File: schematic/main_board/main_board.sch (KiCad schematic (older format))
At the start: 13 parts, among them J1 Line OUT, J2 Line IN, P1 +Vref, P2 GND, P3 -Vref, P4 Probe, P5 GND, U1 LM324N

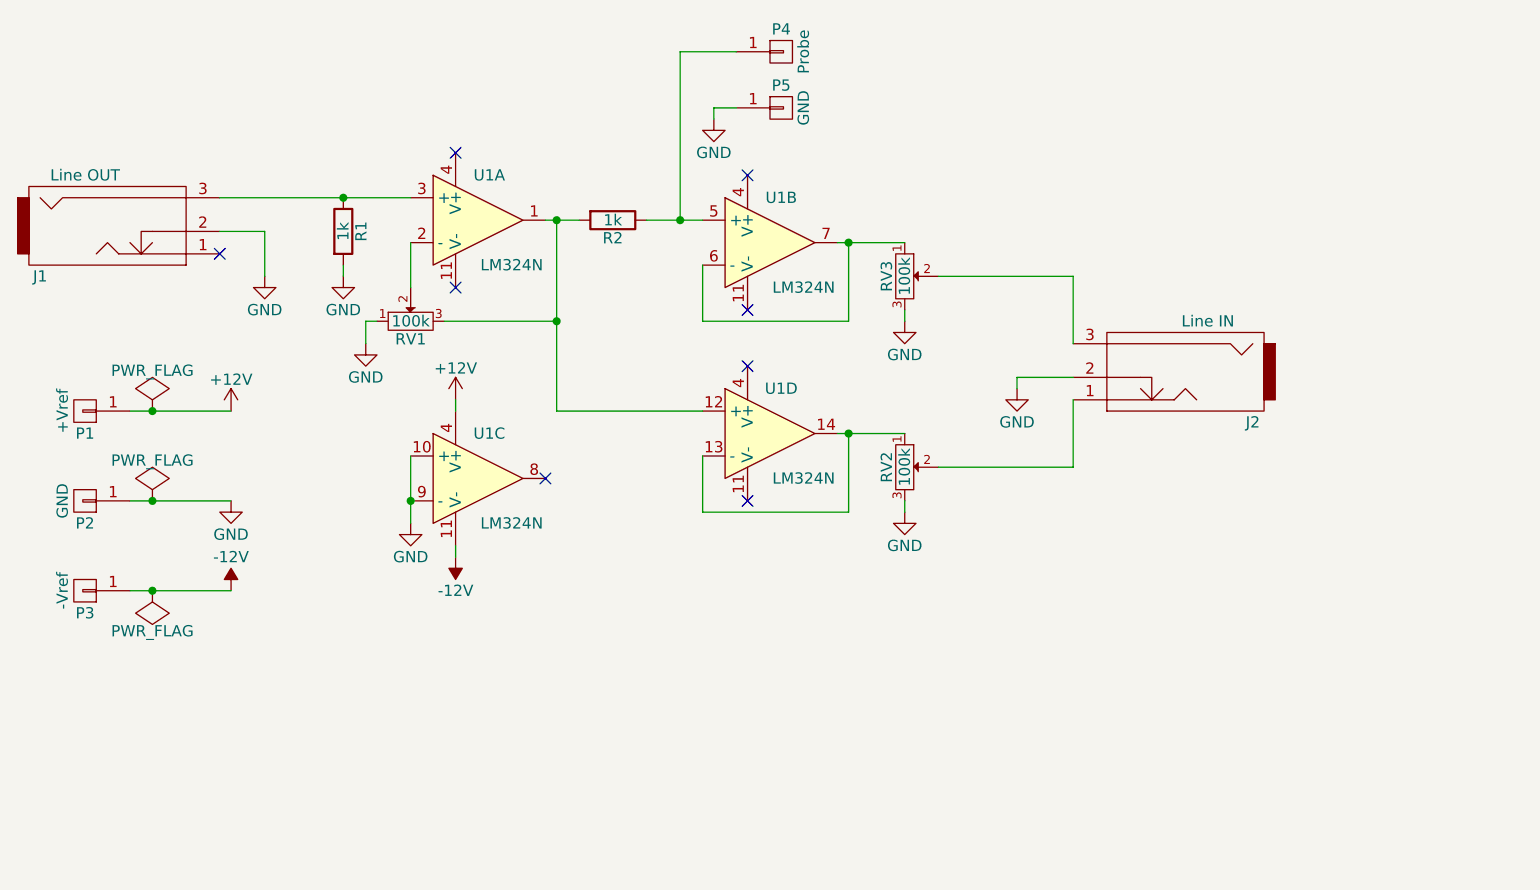
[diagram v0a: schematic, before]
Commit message: Add footprint for potentiometer.
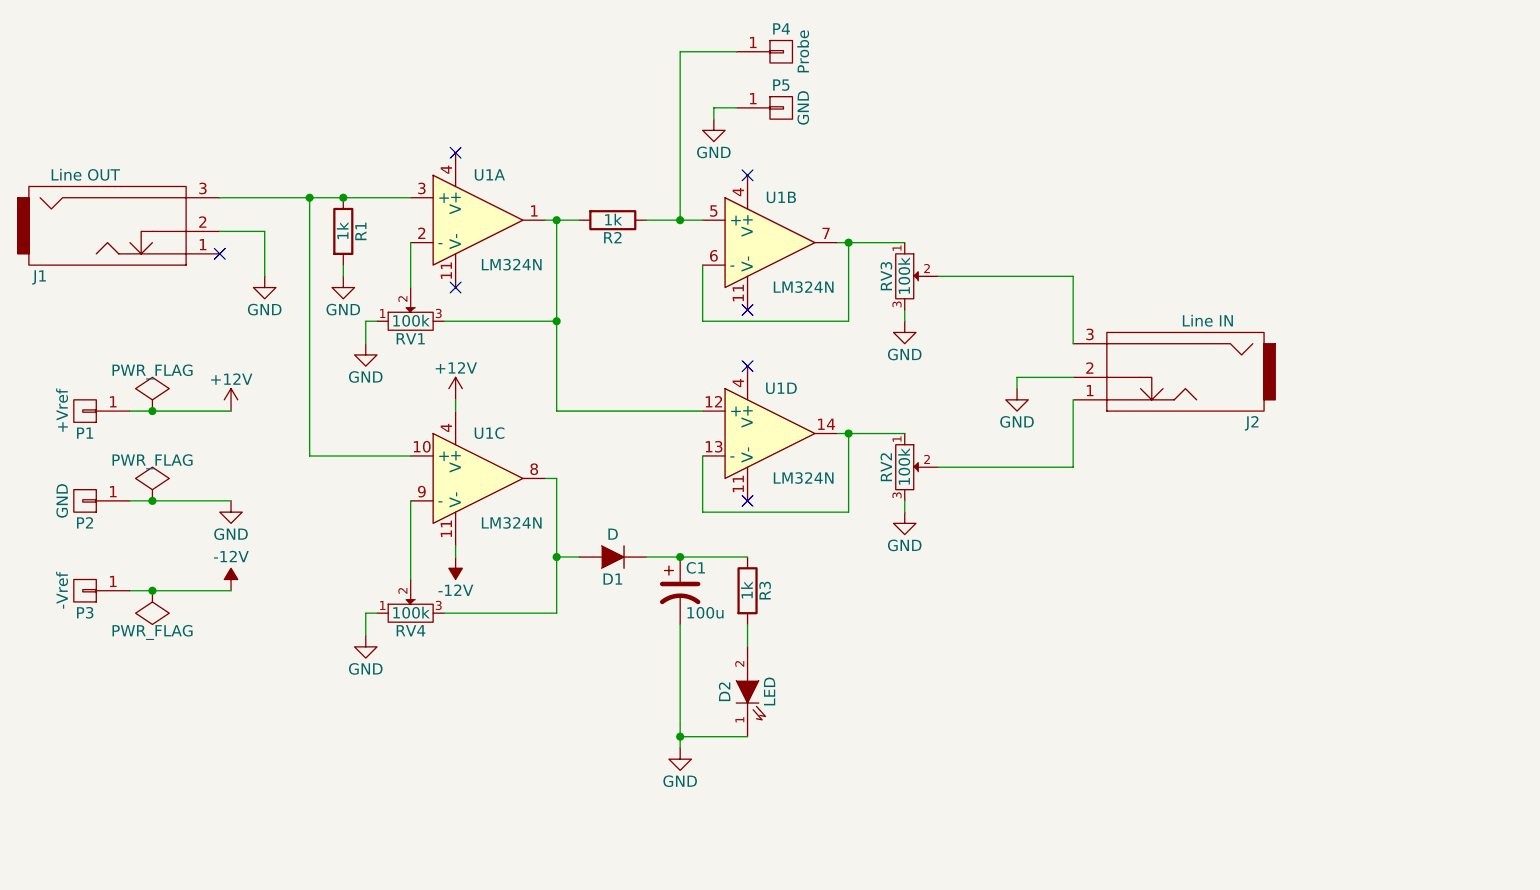
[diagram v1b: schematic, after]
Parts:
- added C1: 100u, symbol CP1
- added D1: D, symbol D
- added D2: LED, symbol LED
- added R3: 1k, footprints:Resistor_Horizontal_RM20mm_0.25W, symbol R
- added RV4: 100k, footprints:Potentiometer_CP3-36, symbol POT
- RV1, RV2, RV3: footprint Potentiometers:Potentiometer_Bourns_3005_Angular_ScrewFront -> footprints:Potentiometer_CP3-36
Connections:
- net GND: now also C1.2, D2.1 (K), RV4.1; no longer U1.10 (+), U1.9 (-)
- net at J1.3, R1.1, U1.3 (+): now also U1.10 (+)
- net at U1.8: now also D1.2 (A), RV4.3
- new net: RV4.2, U1.9 (-)
- new net: C1.1, D1.1 (K), R3.1
- new net: D2.2 (A), R3.2
- no-connect marks 8 -> 7
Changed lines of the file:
@@
 	1    0    0    -1
 $EndComp
-NoConn ~ 4000 3700
 $Comp
 L GND #PWR01
 U 1 1 57BD55DE
-P 3400 3900
-F 0 "#PWR01" H 3400 3650 50  0001 C CNN
-F 1 "GND" H 3400 3750 50  0000 C CNN
-F 2 "" H 3400 3900 50  0000 C CNN
-F 3 "" H 3400 3900 50  0000 C CNN
-	1    3400 3900
+P 3200 4400
+F 0 "#PWR01" H 3200 4150 50  0001 C CNN
+F 1 "GND" H 3200 4250 50  0000 C CNN
+F 2 "" H 3200 4400 50  0000 C CNN
+F 3 "" H 3200 4400 50  0000 C CNN
+	1    3200 4400
 	1    0    0    -1
 $EndComp
@@
 F 0 "RV1" H 3400 2920 50  0000 C CNN
 F 1 "100k" H 3400 3000 50  0000 C CNN
-F 2 "Potentiometers:Potentiometer_Bourns_3005_Angular_ScrewFront" H 3400 3000 50  0001 C CNN
+F 2 "footprints:Potentiometer_CP3-36" H 3400 3000 50  0001 C CNN
 F 3 "" H 3400 3000 50  0000 C CNN
 	1    3400 3000
@@
 F 0 "RV3" H 5600 2720 50  0000 C CNN
 F 1 "100k" H 5600 2800 50  0000 C CNN
-F 2 "Potentiometers:Potentiometer_Bourns_3005_Angular_ScrewFront" H 5600 2800 50  0001 C CNN
+F 2 "footprints:Potentiometer_CP3-36" H 5600 2800 50  0001 C CNN
 F 3 "" H 5600 2800 50  0000 C CNN
 	1    5600 2800
@@
 F 0 "RV2" H 5600 3570 50  0000 C CNN
 F 1 "100k" H 5600 3650 50  0000 C CNN
-F 2 "Potentiometers:Potentiometer_Bourns_3005_Angular_ScrewFront" H 5600 3650 50  0001 C CNN
+F 2 "footprints:Potentiometer_CP3-36" H 5600 3650 50  0001 C CNN
 F 3 "" H 5600 3650 50  0000 C CNN
 	1    5600 3650
@@
 	1    0    0    -1
 $EndComp
-Wire Wire Line
-	5300 2650 5600 2650
-Wire Wire Line
-	4700 2750 4700 3000
-Wire Wire Line
-	4700 3000 5350 3000
-Wire Wire Line
-	5350 3000 5350 2650
-Connection ~ 5350 2650
-Wire Wire Line
-	5600 3500 5300 3500
-Wire Wire Line
-	4700 3600 4700 3850
-Wire Wire Line
-	4700 3850 5350 3850
-Wire Wire Line
-	5350 3850 5350 3500
-Connection ~ 5350 3500
-Wire Wire Line
-	5600 3800 5600 3850
-Wire Wire Line
-	3400 2650 3400 2850
-Wire Wire Line
-	3550 3000 4050 3000
 $Comp
 L GND #PWR04
@@
 	1    0    0    -1
 $EndComp
-Wire Wire Line
-	3200 3100 3200 3000
-Wire Wire Line
-	3200 3000 3250 3000
 $Comp
 L GND #PWR05
@@
 	1    0    0    -1
 $EndComp
-Wire Wire Line
-	3100 2750 3100 2800
-Wire Wire Line
-	2550 2450 3400 2450
-Wire Wire Line
-	4700 2550 4450 2550
-Wire Wire Line
-	4000 2550 4150 2550
-Wire Wire Line
-	4050 2550 4050 3400
-Connection ~ 4050 2550
-Wire Wire Line
-	4050 3400 4700 3400
-Connection ~ 4050 3000
 NoConn ~ 3600 2850
 NoConn ~ 3600 2250
@@
 	-1   0    0    1
 $EndComp
-Wire Wire Line
-	5600 3000 5600 2950
-Wire Wire Line
-	3600 4000 3600 4050
-Wire Wire Line
-	3600 3400 3600 3350
-Wire Wire Line
-	3400 3600 3400 3900
-Connection ~ 3400 3800
 $Comp
 L PWR_FLAG #FLG07
@@
 	1    0    0    -1
 $EndComp
-Wire Wire Line
-	2150 3400 2600 3400
-Connection ~ 2250 3400
 $Comp
 L GND #PWR09
@@
 $EndComp
 $Comp
-L -12V #PWR4
+L -12V #PWR3
 U 1 1 57BD83A0
 P 2600 4200
-F 0 "#PWR4" H 2600 4300 50  0001 C CNN
+F 0 "#PWR3" H 2600 4300 50  0001 C CNN
 F 1 "-12V" H 2600 4350 50  0000 C CNN
 F 2 "" H 2600 4200 50  0000 C CNN
@@
 	-1   0    0    1
 $EndComp
-Wire Wire Line
-	2150 4200 2600 4200
-Connection ~ 2250 4200
-Wire Wire Line
-	2150 3800 2600 3800
-Connection ~ 2250 3800
 $Comp
 L CONN_01X01 P4
@@
 	1    0    0    -1
 $EndComp
-Wire Wire Line
-	4850 2050 4750 2050
-Wire Wire Line
-	4750 2050 4750 2100
-Wire Wire Line
-	4600 1800 4600 2550
-Connection ~ 4600 2550
-Wire Wire Line
-	4850 1800 4600 1800
 $Comp
 L JACK_2P J1
@@
 	1    0    0    -1
 $EndComp
+$Comp
+L D D1
+U 1 1 57C3D329
+P 4300 4050
+F 0 "D1" H 4300 4150 50  0000 C CNN
+F 1 "D" H 4300 3950 50  0000 C CNN
+F 2 "" H 4300 4050 50  0001 C CNN
+F 3 "" H 4300 4050 50  0000 C CNN
+	1    4300 4050
+	-1   0    0    1
+$EndComp
+$Comp
+L R R3
+U 1 1 57C3D3FD
+P 4900 4200
+F 0 "R3" V 4980 4200 50  0000 C CNN
+F 1 "1k" V 4900 4200 50  0000 C CNN
+F 2 "footprints:Resistor_Horizontal_RM20mm_0.25W" V 4830 4200 50  0001 C CNN
+F 3 "" H 4900 4200 50  0000 C CNN
+	1    4900 4200
+	1    0    0    -1
+$EndComp
+$Comp
+L CP1 C1
+U 1 1 57C3D44E
+P 4600 4200
+F 0 "C1" H 4625 4300 50  0000 L CNN
+F 1 "100u" H 4625 4100 50  0000 L CNN
+F 2 "" H 4600 4200 50  0001 C CNN
+F 3 "" H 4600 4200 50  0000 C CNN
+	1    4600 4200
+	1    0    0    -1
+$EndComp
+$Comp
+L LED D2
+U 1 1 57C3D493
+P 4900 4650
+F 0 "D2" H 4900 4750 50  0000 C CNN
+F 1 "LED" H 4900 4550 50  0000 C CNN
+F 2 "" H 4900 4650 50  0001 C CNN
+F 3 "" H 4900 4650 50  0000 C CNN
+	1    4900 4650
+	0    -1   -1   0
+$EndComp
+$Comp
+L POT RV4
+U 1 1 57C3E022
+P 3400 4300
+F 0 "RV4" H 3400 4220 50  0000 C CNN
+F 1 "100k" H 3400 4300 50  0000 C CNN
+F 2 "footprints:Potentiometer_CP3-36" H 3400 4300 50  0001 C CNN
+F 3 "" H 3400 4300 50  0000 C CNN
+	1    3400 4300
+	1    0    0    -1
+$EndComp
+$Comp
+L GND #PWR015
+U 1 1 57C3EFA0
+P 4600 4900
+F 0 "#PWR015" H 4600 4650 50  0001 C CNN
+F 1 "GND" H 4600 4750 50  0000 C CNN
+F 2 "" H 4600 4900 50  0000 C CNN
+F 3 "" H 4600 4900 50  0000 C CNN
+	1    4600 4900
+	1    0    0    -1
+$EndComp
+Wire Wire Line
+	5300 2650 5600 2650
+Wire Wire Line
+	4700 2750 4700 3000
+Wire Wire Line
+	4700 3000 5350 3000
+Wire Wire Line
+	5350 3000 5350 2650
+Connection ~ 5350 2650
+Wire Wire Line
+	5600 3500 5300 3500
+Wire Wire Line
+	4700 3600 4700 3850
+Wire Wire Line
+	4700 3850 5350 3850
+Wire Wire Line
+	5350 3850 5350 3500
+Connection ~ 5350 3500
+Wire Wire Line
+	5600 3800 5600 3850
+Wire Wire Line
+	3400 2650 3400 2850
+Wire Wire Line
+	3550 3000 4050 3000
+Wire Wire Line
+	3200 3100 3200 3000
+Wire Wire Line
+	3200 3000 3250 3000
+Wire Wire Line
+	3100 2750 3100 2800
+Wire Wire Line
+	2550 2450 3400 2450
+Wire Wire Line
+	4700 2550 4450 2550
+Wire Wire Line
+	4000 2550 4150 2550
+Wire Wire Line
+	4050 2550 4050 3400
+Connection ~ 4050 2550
+Wire Wire Line
+	4050 3400 4700 3400
+Connection ~ 4050 3000
+Wire Wire Line
+	5600 3000 5600 2950
+Wire Wire Line
+	3600 4000 3600 4050
+Wire Wire Line
+	3600 3400 3600 3350
+Wire Wire Line
+	2150 3400 2600 3400
+Connection ~ 2250 3400
+Wire Wire Line
+	2150 4200 2600 4200
+Connection ~ 2250 4200
+Wire Wire Line
+	2150 3800 2600 3800
+Connection ~ 2250 3800
+Wire Wire Line
+	4850 2050 4750 2050
+Wire Wire Line
+	4750 2050 4750 2100
+Wire Wire Line
+	4600 1800 4600 2550
+Connection ~ 4600 2550
+Wire Wire Line
+	4850 1800 4600 1800
 Wire Wire Line
 	6350 3250 6100 3250
@@
 	2750 2600 2550 2600
 Connection ~ 3100 2450
+Wire Wire Line
+	3400 3800 3400 4150
+Wire Wire Line
+	3200 4400 3200 4300
+Wire Wire Line
+	3200 4300 3250 4300
+Wire Wire Line
+	3550 4300 4050 4300
+Wire Wire Line
+	4050 4300 4050 3700
+Wire Wire Line
+	4050 3700 4000 3700
+Wire Wire Line
+	2950 2450 2950 3600
+Wire Wire Line
+	2950 3600 3400 3600
+Connection ~ 2950 2450
+Wire Wire Line
+	4150 4050 4050 4050
+Connection ~ 4050 4050
+Wire Wire Line
+	4450 4050 4900 4050
+Connection ~ 4600 4050
+Wire Wire Line
+	4900 4350 4900 4450
+Wire Wire Line
+	4900 4850 4600 4850
+Wire Wire Line
+	4600 4350 4600 4900
+Connection ~ 4600 4850
 $EndSCHEMATC

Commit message: Added circuit to schematic for limit output voltage range.
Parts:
- added D3, D4, D5, D6: D, symbol D
- added R4, R5: 1k, symbol R
- J1: value Line OUT -> To Line OUT
- J2: value Line IN -> To Line IN
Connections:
- net GND: now also RV2.1, RV3.1, D3.1 (K), D4.1 (K), D5.2 (A), D6.2 (A); no longer RV2.3, RV3.3
- net at U1.6 (-), U1.7: now also RV3.3; no longer RV3.1
- net at U1.13 (-), U1.14: now also RV2.3; no longer RV2.1
- net at RV3.2: now also R4.2; no longer J2.3
- net at RV2.2: now also R5.2; no longer J2.1
- new net: D4.2 (A), D6.1 (K), J2.1, R5.1
- new net: D3.2 (A), D5.1 (K), J2.3, R4.1
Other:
- moved on the sheet: J2
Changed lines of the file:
@@
 $EndComp
 $Comp
-L GND #PWR01
+L GND #PWR7
 U 1 1 57BD55DE
 P 3200 4400
-F 0 "#PWR01" H 3200 4150 50  0001 C CNN
+F 0 "#PWR7" H 3200 4150 50  0001 C CNN
 F 1 "GND" H 3200 4250 50  0000 C CNN
 F 2 "" H 3200 4400 50  0000 C CNN
@@
 F 3 "" H 5600 2800 50  0000 C CNN
 	1    5600 2800
-	0    1    1    0
+	0    1    -1   0
 $EndComp
 $Comp
@@
 F 3 "" H 5600 3650 50  0000 C CNN
 	1    5600 3650
-	0    1    1    0
-$EndComp
-$Comp
-L GND #PWR02
+	0    1    -1   0
+$EndComp
+$Comp
+L GND #PWR12
 U 1 1 57BD5FBC
 P 5600 3000
-F 0 "#PWR02" H 5600 2750 50  0001 C CNN
+F 0 "#PWR12" H 5600 2750 50  0001 C CNN
 F 1 "GND" H 5600 2850 50  0000 C CNN
 F 2 "" H 5600 3000 50  0000 C CNN
@@
 $EndComp
 $Comp
-L GND #PWR03
+L GND #PWR13
 U 1 1 57BD6135
 P 5600 3850
-F 0 "#PWR03" H 5600 3600 50  0001 C CNN
+F 0 "#PWR13" H 5600 3600 50  0001 C CNN
 F 1 "GND" H 5600 3700 50  0000 C CNN
 F 2 "" H 5600 3850 50  0000 C CNN
@@
 $EndComp
 $Comp
-L GND #PWR04
+L GND #PWR6
 U 1 1 57BD62A5
 P 3200 3100
-F 0 "#PWR04" H 3200 2850 50  0001 C CNN
+F 0 "#PWR6" H 3200 2850 50  0001 C CNN
 F 1 "GND" H 3200 2950 50  0000 C CNN
 F 2 "" H 3200 3100 50  0000 C CNN
@@
 $EndComp
 $Comp
-L GND #PWR05
+L GND #PWR5
 U 1 1 57BD632F
 P 3100 2800
-F 0 "#PWR05" H 3100 2550 50  0001 C CNN
+F 0 "#PWR5" H 3100 2550 50  0001 C CNN
 F 1 "GND" H 3100 2650 50  0000 C CNN
 F 2 "" H 3100 2800 50  0000 C CNN
@@
 NoConn ~ 4900 3800
 $Comp
-L +12V #PWR06
+L +12V #PWR8
 U 1 1 57BD6625
 P 3600 3350
-F 0 "#PWR06" H 3600 3200 50  0001 C CNN
+F 0 "#PWR8" H 3600 3200 50  0001 C CNN
 F 1 "+12V" H 3600 3490 50  0000 C CNN
 F 2 "" H 3600 3350 50  0000 C CNN
@@
 $EndComp
 $Comp
-L PWR_FLAG #FLG07
+L PWR_FLAG #FLG1
 U 1 1 57BD744C
 P 2250 3400
-F 0 "#FLG07" H 2250 3495 50  0001 C CNN
+F 0 "#FLG1" H 2250 3495 50  0001 C CNN
 F 1 "PWR_FLAG" H 2250 3580 50  0000 C CNN
 F 2 "" H 2250 3400 50  0000 C CNN
@@
 $EndComp
 $Comp
-L +12V #PWR08
+L +12V #PWR1
 U 1 1 57BD755B
 P 2600 3400
-F 0 "#PWR08" H 2600 3250 50  0001 C CNN
+F 0 "#PWR1" H 2600 3250 50  0001 C CNN
 F 1 "+12V" H 2600 3540 50  0000 C CNN
 F 2 "" H 2600 3400 50  0000 C CNN
@@
 $EndComp
 $Comp
-L GND #PWR09
+L GND #PWR2
 U 1 1 57BD8243
 P 2600 3800
-F 0 "#PWR09" H 2600 3550 50  0001 C CNN
+F 0 "#PWR2" H 2600 3550 50  0001 C CNN
 F 1 "GND" H 2600 3650 50  0000 C CNN
 F 2 "" H 2600 3800 50  0000 C CNN
@@
 $EndComp
 $Comp
-L PWR_FLAG #FLG010
+L PWR_FLAG #FLG2
 U 1 1 57BD83E4
 P 2250 3800
-F 0 "#FLG010" H 2250 3895 50  0001 C CNN
+F 0 "#FLG2" H 2250 3895 50  0001 C CNN
 F 1 "PWR_FLAG" H 2250 3980 50  0000 C CNN
 F 2 "" H 2250 3800 50  0000 C CNN
@@
 $EndComp
 $Comp
-L PWR_FLAG #FLG011
+L PWR_FLAG #FLG3
 U 1 1 57BD841C
 P 2250 4200
-F 0 "#FLG011" H 2250 4295 50  0001 C CNN
+F 0 "#FLG3" H 2250 4295 50  0001 C CNN
 F 1 "PWR_FLAG" H 2250 4380 50  0000 C CNN
 F 2 "" H 2250 4200 50  0000 C CNN
@@
 $EndComp
 $Comp
-L GND #PWR012
+L GND #PWR11
 U 1 1 57BD887B
 P 4750 2100
-F 0 "#PWR012" H 4750 1850 50  0001 C CNN
+F 0 "#PWR11" H 4750 1850 50  0001 C CNN
 F 1 "GND" H 4750 1950 50  0000 C CNN
 F 2 "" H 4750 2100 50  0000 C CNN
@@
 P 2100 2600
 F 0 "J1" H 1750 2400 50  0000 C CNN
-F 1 "Line OUT" H 1950 2850 50  0000 C CNN
+F 1 "To Line OUT" H 1950 2850 50  0000 C CNN
 F 2 "Connect:PINHEAD1-3" H 2100 2600 50  0001 C CNN
 F 3 "" H 2100 2600 50  0000 C CNN
@@
 L JACK_2P J2
 U 1 1 57BD94A5
-P 6800 3250
-F 0 "J2" H 6450 3050 50  0000 C CNN
-F 1 "Line IN" H 6650 3500 50  0000 C CNN
-F 2 "Connect:PINHEAD1-3" H 6800 3250 50  0001 C CNN
-F 3 "" H 6800 3250 50  0000 C CNN
-	1    6800 3250
+P 7400 3250
+F 0 "J2" H 7050 3050 50  0000 C CNN
+F 1 "To Line IN" H 7250 3500 50  0000 C CNN
+F 2 "Connect:PINHEAD1-3" H 7400 3250 50  0001 C CNN
+F 3 "" H 7400 3250 50  0000 C CNN
+	1    7400 3250
 	-1   0    0    -1
 $EndComp
 NoConn ~ 2550 2700
 $Comp
-L GND #PWR013
+L GND #PWR4
 U 1 1 57BD9647
 P 2750 2800
-F 0 "#PWR013" H 2750 2550 50  0001 C CNN
+F 0 "#PWR4" H 2750 2550 50  0001 C CNN
 F 1 "GND" H 2750 2650 50  0000 C CNN
 F 2 "" H 2750 2800 50  0000 C CNN
@@
 $EndComp
 $Comp
-L GND #PWR014
+L GND #PWR14
 U 1 1 57BD96EB
-P 6100 3300
-F 0 "#PWR014" H 6100 3050 50  0001 C CNN
-F 1 "GND" H 6100 3150 50  0000 C CNN
-F 2 "" H 6100 3300 50  0000 C CNN
-F 3 "" H 6100 3300 50  0000 C CNN
-	1    6100 3300
+P 6750 3350
+F 0 "#PWR14" H 6750 3100 50  0001 C CNN
+F 1 "GND" H 6750 3200 50  0000 C CNN
+F 2 "" H 6750 3350 50  0000 C CNN
+F 3 "" H 6750 3350 50  0000 C CNN
+	1    6750 3350
 	1    0    0    -1
 $EndComp
@@
 $EndComp
 $Comp
-L GND #PWR015
+L GND #PWR10
 U 1 1 57C3EFA0
 P 4600 4900
-F 0 "#PWR015" H 4600 4650 50  0001 C CNN
+F 0 "#PWR10" H 4600 4650 50  0001 C CNN
 F 1 "GND" H 4600 4750 50  0000 C CNN
 F 2 "" H 4600 4900 50  0000 C CNN
@@
 	1    0    0    -1
 $EndComp
+$Comp
+L R R4
+U 1 1 57C5790E
+P 5950 2800
+F 0 "R4" V 6030 2800 50  0000 C CNN
+F 1 "1k" V 5950 2800 50  0000 C CNN
+F 2 "" V 5880 2800 50  0000 C CNN
+F 3 "" H 5950 2800 50  0000 C CNN
+	1    5950 2800
+	0    1    1    0
+$EndComp
+$Comp
+L R R5
+U 1 1 57C57CFF
+P 5950 3650
+F 0 "R5" V 6030 3650 50  0000 C CNN
+F 1 "1k" V 5950 3650 50  0000 C CNN
+F 2 "" V 5880 3650 50  0000 C CNN
+F 3 "" H 5950 3650 50  0000 C CNN
+	1    5950 3650
+	0    1    1    0
+$EndComp
+$Comp
+L D D5
+U 1 1 57C57DD5
+P 6500 2950
+F 0 "D5" H 6500 3050 50  0000 C CNN
+F 1 "D" H 6500 2850 50  0000 C CNN
+F 2 "" H 6500 2950 50  0000 C CNN
+F 3 "" H 6500 2950 50  0000 C CNN
+	1    6500 2950
+	0    1    1    0
+$EndComp
+$Comp
+L D D4
+U 1 1 57C57E7E
+P 6250 3500
+F 0 "D4" H 6250 3600 50  0000 C CNN
+F 1 "D" H 6250 3400 50  0000 C CNN
+F 2 "" H 6250 3500 50  0000 C CNN
+F 3 "" H 6250 3500 50  0000 C CNN
+	1    6250 3500
+	0    1    1    0
+$EndComp
+$Comp
+L D D3
+U 1 1 57C57F60
+P 6250 2950
+F 0 "D3" H 6250 3050 50  0000 C CNN
+F 1 "D" H 6250 2850 50  0000 C CNN
+F 2 "" H 6250 2950 50  0000 C CNN
+F 3 "" H 6250 2950 50  0000 C CNN
+	1    6250 2950
+	0    -1   -1   0
+$EndComp
+$Comp
+L D D6
+U 1 1 57C57FE3
+P 6500 3500
+F 0 "D6" H 6500 3600 50  0000 C CNN
+F 1 "D" H 6500 3400 50  0000 C CNN
+F 2 "" H 6500 3500 50  0000 C CNN
+F 3 "" H 6500 3500 50  0000 C CNN
+	1    6500 3500
+	0    -1   -1   0
+$EndComp
 Wire Wire Line
 	5300 2650 5600 2650
@@
 	4850 1800 4600 1800
 Wire Wire Line
-	6350 3250 6100 3250
-Wire Wire Line
-	6100 3250 6100 3300
-Wire Wire Line
-	5750 3650 6350 3650
-Wire Wire Line
-	6350 3650 6350 3350
-Wire Wire Line
-	5750 2800 6350 2800
-Wire Wire Line
-	6350 2800 6350 3100
+	6950 3650 6950 3350
+Wire Wire Line
+	6950 2800 6950 3100
 Wire Wire Line
 	2750 2800 2750 2600
@@
 	4600 4350 4600 4900
 Connection ~ 4600 4850
+Wire Wire Line
+	5800 3650 5750 3650
+Wire Wire Line
+	5800 2800 5750 2800
+Wire Wire Line
+	6100 2800 6950 2800
+Connection ~ 6250 2800
+Connection ~ 6500 2800
+Wire Wire Line
+	6100 3650 6950 3650
+Connection ~ 6500 3650
+Connection ~ 6250 3650
+Wire Wire Line
+	6250 3350 6250 3300
+Wire Wire Line
+	6250 3300 6750 3300
+Wire Wire Line
+	6500 3100 6500 3350
+Wire Wire Line
+	6250 3100 6250 3150
+Wire Wire Line
+	6250 3150 6500 3150
+Connection ~ 6500 3300
+Connection ~ 6500 3150
+Wire Wire Line
+	6750 3250 6750 3350
+Wire Wire Line
+	6950 3250 6750 3250
+Connection ~ 6750 3300
 $EndSCHEMATC
